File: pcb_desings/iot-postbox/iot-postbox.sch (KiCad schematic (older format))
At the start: 3 parts

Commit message: Added board sch with 2 inputs for restart esp12
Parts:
- removed J?: XLR3_Switched, symbol Connector:XLR3_Switched
- removed U?: WeMos_mini, symbol wemos_mini:WeMos_mini
- added C1: 10uF, Capacitor_SMD:C_0805_2012Metric, symbol Device:C
- added C2: 100nF, Capacitor_SMD:C_0805_2012Metric, symbol Device:C
- added D1, D2, D3: 1N4007, Diode_SMD:D_SOD-123, symbol Device:D
- added J1: Switch_1, Connector_PinHeader_2.54mm:PinHeader_1x02_P2.54mm_Vertical, symbol Connector_Generic:Conn_01x02
- added J2: Switch_2, Connector_PinHeader_2.54mm:PinHeader_1x02_P2.54mm_Vertical, symbol Connector_Generic:Conn_01x02
- added J3: Battery, Connector_PinHeader_2.54mm:PinHeader_1x02_P2.54mm_Vertical, symbol Connector_Generic:Conn_01x02
- added R2, R3, R4, R5, R6, R7: 10k, Resistor_SMD:R_0805_2012Metric, symbol Device:R
- added U1: ESP-12F, RF_Module:ESP-12E, symbol RF_Module:ESP-12F
- R1: footprint (none) -> Resistor_SMD:R_0805_2012Metric
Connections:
- net labels added: +3V3, CH_PD, GPIO12, GPIO13, GPIO14, VCC
- wire segments 9 -> 55
- no-connect marks 0 -> 12

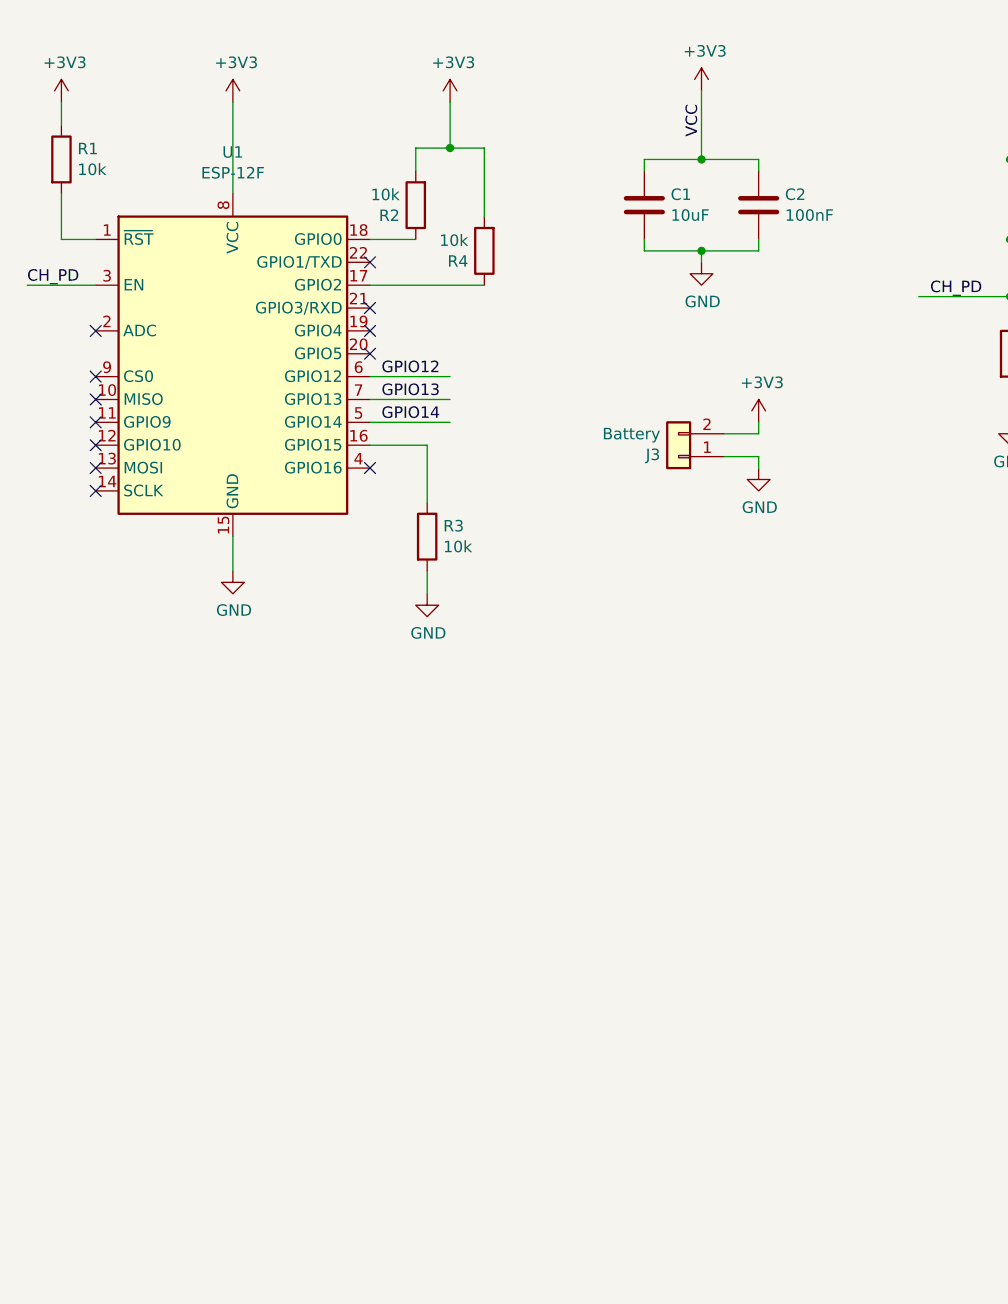
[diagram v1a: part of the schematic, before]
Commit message: Added uart connection to board sch
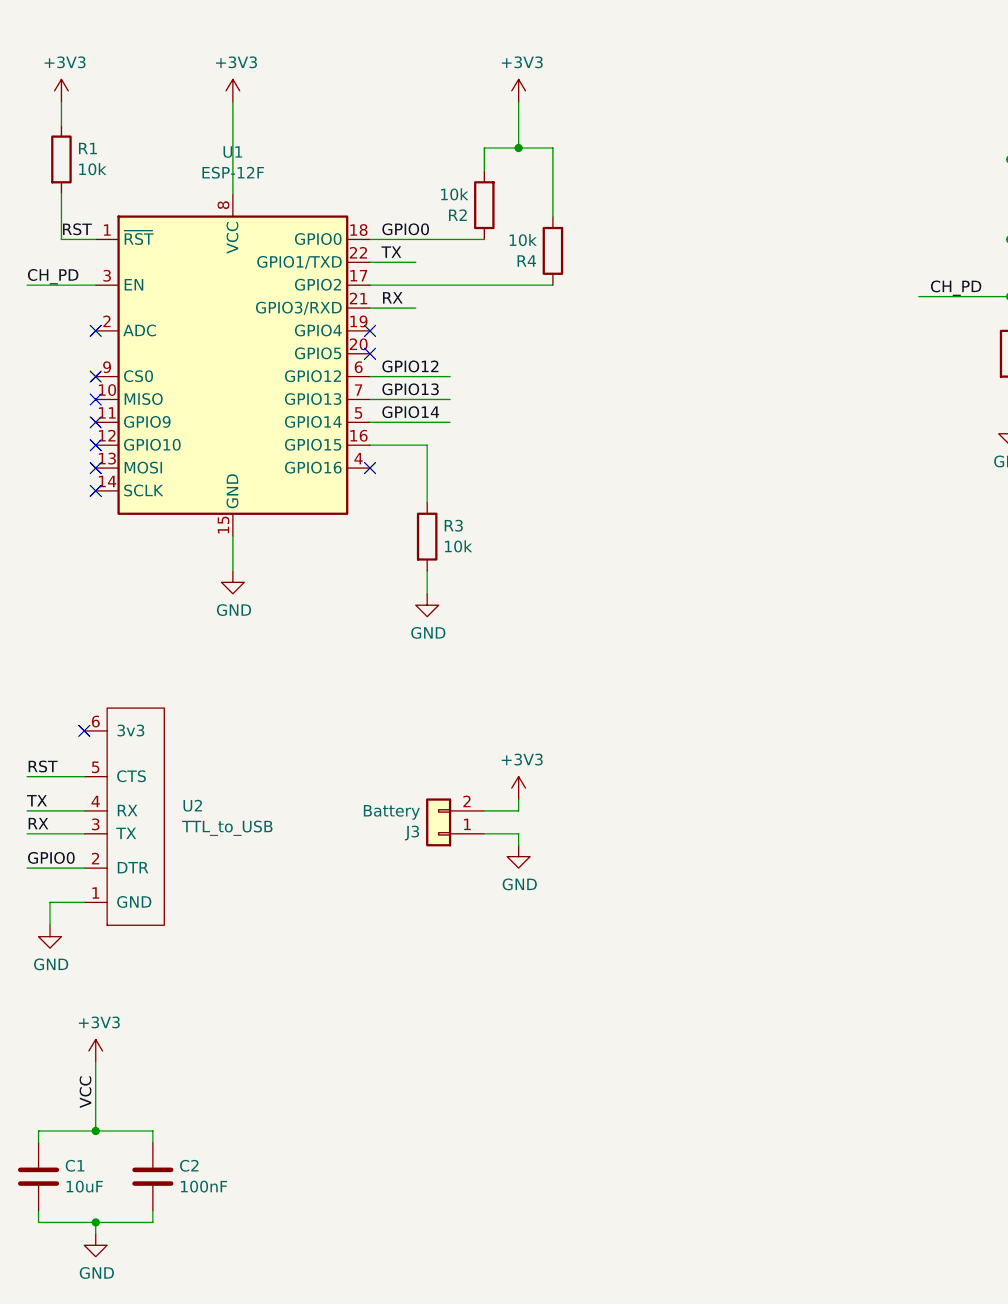
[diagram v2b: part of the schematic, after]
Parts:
- added U2: TTL_to_USB, Connector_PinHeader_2.54mm:PinHeader_1x06_P2.54mm_Vertical, symbol iot-postbox:TTL_to_USB
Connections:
- net labels added: GPIO0, RST, RX, TX
- wire segments 55 -> 63
- no-connect marks 12 -> 11
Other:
- moved on the sheet: C1, C2, J3, R2, R4
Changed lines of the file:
@@
 Comment4 ""
 $EndDescr
-$Comp
-L RF_Module:ESP-12F U1
-U 1 1 60AE687C
-P 1950 2350
-F 0 "U1" H 1950 3331 50  0000 C CNN
-F 1 "ESP-12F" H 1950 3240 50  0000 C CNN
-F 2 "RF_Module:ESP-12E" H 1950 2350 50  0001 C CNN
-F 3 "http://wiki.ai-thinker.com/_media/esp8266/esp8266_series_modules_user_manual_v1.1.pdf" H 1600 2450 50  0001 C CNN
-	1    1950 2350
-	1    0    0    -1
-$EndComp
 Wire Wire Line
 	1350 1950 1050 1950
@@
 L power:+3V3 #PWR06
 U 1 1 60B15876
-P 4000 1100
-F 0 "#PWR06" H 4000 950 50  0001 C CNN
-F 1 "+3V3" H 4015 1273 50  0000 C CNN
-F 2 "" H 4000 1100 50  0001 C CNN
-F 3 "" H 4000 1100 50  0001 C CNN
-	1    4000 1100
+P 1350 5350
+F 0 "#PWR06" H 1350 5200 50  0001 C CNN
+F 1 "+3V3" H 1365 5523 50  0000 C CNN
+F 2 "" H 1350 5350 50  0001 C CNN
+F 3 "" H 1350 5350 50  0001 C CNN
+	1    1350 5350
 	1    0    0    -1
 $EndComp
@@
 Wire Wire Line
 	8150 1950 8150 2150
-Wire Wire Line
-	2550 1750 2750 1750
 $Comp
 L Device:R R2
 U 1 1 60B5027F
-P 2750 1600
-F 0 "R2" H 2820 1646 50  0000 L CNN
-F 1 "10k" H 2820 1555 50  0000 L CNN
-F 2 "Resistor_SMD:R_0805_2012Metric" V 2680 1600 50  0001 C CNN
-F 3 "~" H 2750 1600 50  0001 C CNN
-	1    2750 1600
+P 3050 1600
+F 0 "R2" H 3120 1646 50  0000 L CNN
+F 1 "10k" H 3120 1555 50  0000 L CNN
+F 2 "Resistor_SMD:R_0805_2012Metric" V 2980 1600 50  0001 C CNN
+F 3 "~" H 3050 1600 50  0001 C CNN
+	1    3050 1600
 	-1   0    0    1
 $EndComp
@@
 L Device:R R4
 U 1 1 60B50B9E
-P 3050 1800
-F 0 "R4" H 3120 1846 50  0000 L CNN
-F 1 "10k" H 3120 1755 50  0000 L CNN
-F 2 "Resistor_SMD:R_0805_2012Metric" V 2980 1800 50  0001 C CNN
-F 3 "~" H 3050 1800 50  0001 C CNN
-	1    3050 1800
+P 3350 1800
+F 0 "R4" H 3420 1846 50  0000 L CNN
+F 1 "10k" H 3420 1755 50  0000 L CNN
+F 2 "Resistor_SMD:R_0805_2012Metric" V 3280 1800 50  0001 C CNN
+F 3 "~" H 3350 1800 50  0001 C CNN
+	1    3350 1800
 	-1   0    0    1
 $EndComp
 Wire Wire Line
-	2550 1950 3050 1950
-Wire Wire Line
-	2750 1450 2750 1350
-Wire Wire Line
-	3050 1350 3050 1650
-Wire Wire Line
-	2750 1350 2900 1350
+	3050 1450 3050 1350
+Wire Wire Line
+	3350 1350 3350 1650
+Wire Wire Line
+	3050 1350 3200 1350
 $Comp
 L power:+3V3 #PWR05
 U 1 1 60B58812
-P 2900 1150
-F 0 "#PWR05" H 2900 1000 50  0001 C CNN
-F 1 "+3V3" H 2915 1323 50  0000 C CNN
-F 2 "" H 2900 1150 50  0001 C CNN
-F 3 "" H 2900 1150 50  0001 C CNN
-	1    2900 1150
-	1    0    0    -1
-$EndComp
-Wire Wire Line
-	2900 1150 2900 1350
-Connection ~ 2900 1350
-Wire Wire Line
-	2900 1350 3050 1350
+P 3200 1150
+F 0 "#PWR05" H 3200 1000 50  0001 C CNN
+F 1 "+3V3" H 3215 1323 50  0000 C CNN
+F 2 "" H 3200 1150 50  0001 C CNN
+F 3 "" H 3200 1150 50  0001 C CNN
+	1    3200 1150
+	1    0    0    -1
+$EndComp
+Wire Wire Line
+	3200 1150 3200 1350
+Connection ~ 3200 1350
+Wire Wire Line
+	3200 1350 3350 1350
 $Comp
 L Connector_Generic:Conn_01x02 J2
@@
 	1    0    0    -1
 $EndComp
-Wire Wire Line
-	1950 1550 1950 1150
-Text Label 4000 1300 1    50   ~ 0
+Text Label 1350 5550 1    50   ~ 0
 VCC
 $Comp
 L Device:C C2
 U 1 1 60B72B1E
-P 4250 1600
-F 0 "C2" H 4365 1646 50  0000 L CNN
-F 1 "100nF" H 4365 1555 50  0000 L CNN
-F 2 "Capacitor_SMD:C_0805_2012Metric" H 4288 1450 50  0001 C CNN
-F 3 "~" H 4250 1600 50  0001 C CNN
-	1    4250 1600
-	1    0    0    -1
-$EndComp
-Wire Wire Line
-	4000 1100 4000 1400
-Wire Wire Line
-	4250 1450 4250 1400
-Wire Wire Line
-	4250 1800 4250 1750
+P 1600 5850
+F 0 "C2" H 1715 5896 50  0000 L CNN
+F 1 "100nF" H 1715 5805 50  0000 L CNN
+F 2 "Capacitor_SMD:C_0805_2012Metric" H 1638 5700 50  0001 C CNN
+F 3 "~" H 1600 5850 50  0001 C CNN
+	1    1600 5850
+	1    0    0    -1
+$EndComp
+Wire Wire Line
+	1350 5350 1350 5650
+Wire Wire Line
+	1600 5700 1600 5650
+Wire Wire Line
+	1600 6050 1600 6000
 $Comp
 L power:GND #PWR07
 U 1 1 60B760F1
-P 4000 1850
-F 0 "#PWR07" H 4000 1600 50  0001 C CNN
-F 1 "GND" H 4005 1677 50  0000 C CNN
-F 2 "" H 4000 1850 50  0001 C CNN
-F 3 "" H 4000 1850 50  0001 C CNN
-	1    4000 1850
-	1    0    0    -1
-$EndComp
-Wire Wire Line
-	4000 1850 4000 1800
-Wire Wire Line
-	3750 1750 3750 1800
-Wire Wire Line
-	3750 1450 3750 1400
+P 1350 6100
+F 0 "#PWR07" H 1350 5850 50  0001 C CNN
+F 1 "GND" H 1355 5927 50  0000 C CNN
+F 2 "" H 1350 6100 50  0001 C CNN
+F 3 "" H 1350 6100 50  0001 C CNN
+	1    1350 6100
+	1    0    0    -1
+$EndComp
+Wire Wire Line
+	1350 6100 1350 6050
+Wire Wire Line
+	1100 6000 1100 6050
+Wire Wire Line
+	1100 5700 1100 5650
 $Comp
 L Device:C C1
 U 1 1 60B6FA1D
-P 3750 1600
-F 0 "C1" H 3865 1646 50  0000 L CNN
-F 1 "10uF" H 3865 1555 50  0000 L CNN
-F 2 "Capacitor_SMD:C_0805_2012Metric" H 3788 1450 50  0001 C CNN
-F 3 "~" H 3750 1600 50  0001 C CNN
-	1    3750 1600
-	1    0    0    -1
-$EndComp
-Wire Wire Line
-	3750 1800 4000 1800
-Wire Wire Line
-	3750 1400 4000 1400
-Wire Wire Line
-	4000 1400 4250 1400
-Connection ~ 4000 1400
-Wire Wire Line
-	4000 1800 4250 1800
-Connection ~ 4000 1800
+P 1100 5850
+F 0 "C1" H 1215 5896 50  0000 L CNN
+F 1 "10uF" H 1215 5805 50  0000 L CNN
+F 2 "Capacitor_SMD:C_0805_2012Metric" H 1138 5700 50  0001 C CNN
+F 3 "~" H 1100 5850 50  0001 C CNN
+	1    1100 5850
+	1    0    0    -1
+$EndComp
+Wire Wire Line
+	1100 6050 1350 6050
+Wire Wire Line
+	1100 5650 1350 5650
+Wire Wire Line
+	1350 5650 1600 5650
+Connection ~ 1350 5650
+Wire Wire Line
+	1350 6050 1600 6050
+Connection ~ 1350 6050
 $Comp
 L power:+3V3 #PWR02
@@
 	1    0    0    -1
 $EndComp
-NoConn ~ 2550 1850
-NoConn ~ 2550 2050
 NoConn ~ 2550 2150
 NoConn ~ 2550 2250
@@
 L Connector_Generic:Conn_01x02 J3
 U 1 1 60BC9D92
-P 3900 2700
-F 0 "J3" H 3980 2692 50  0000 L CNN
-F 1 "Battery" H 3980 2601 50  0000 L CNN
-F 2 "Connector_PinHeader_2.54mm:PinHeader_1x02_P2.54mm_Vertical" H 3900 2700 50  0001 C CNN
-F 3 "~" H 3900 2700 50  0001 C CNN
-	1    3900 2700
+P 2850 4350
+F 0 "J3" H 2930 4342 50  0000 L CNN
+F 1 "Battery" H 2930 4251 50  0000 L CNN
+F 2 "Connector_PinHeader_2.54mm:PinHeader_1x02_P2.54mm_Vertical" H 2850 4350 50  0001 C CNN
+F 3 "~" H 2850 4350 50  0001 C CNN
+	1    2850 4350
 	-1   0    0    1
 $EndComp
@@
 L power:+3V3 #PWR013
 U 1 1 60BCAC94
-P 4250 2550
-F 0 "#PWR013" H 4250 2400 50  0001 C CNN
-F 1 "+3V3" H 4265 2723 50  0000 C CNN
-F 2 "" H 4250 2550 50  0001 C CNN
-F 3 "" H 4250 2550 50  0001 C CNN
-	1    4250 2550
+P 3200 4200
+F 0 "#PWR013" H 3200 4050 50  0001 C CNN
+F 1 "+3V3" H 3215 4373 50  0000 C CNN
+F 2 "" H 3200 4200 50  0001 C CNN
+F 3 "" H 3200 4200 50  0001 C CNN
+	1    3200 4200
 	1    0    0    -1
 $EndComp
@@
 L power:GND #PWR014
 U 1 1 60BCB652
-P 4250 2750
-F 0 "#PWR014" H 4250 2500 50  0001 C CNN
-F 1 "GND" H 4255 2577 50  0000 C CNN
-F 2 "" H 4250 2750 50  0001 C CNN
-F 3 "" H 4250 2750 50  0001 C CNN
-	1    4250 2750
-	1    0    0    -1
-$EndComp
-Wire Wire Line
-	4100 2600 4250 2600
-Wire Wire Line
-	4250 2600 4250 2550
-Wire Wire Line
-	4250 2750 4250 2700
-Wire Wire Line
-	4250 2700 4100 2700
+P 3200 4400
+F 0 "#PWR014" H 3200 4150 50  0001 C CNN
+F 1 "GND" H 3205 4227 50  0000 C CNN
+F 2 "" H 3200 4400 50  0001 C CNN
+F 3 "" H 3200 4400 50  0001 C CNN
+	1    3200 4400
+	1    0    0    -1
+$EndComp
+Wire Wire Line
+	3050 4250 3200 4250
+Wire Wire Line
+	3200 4250 3200 4200
+Wire Wire Line
+	3200 4400 3200 4350
+Wire Wire Line
+	3200 4350 3050 4350
+$Comp
+L iot-postbox:TTL_to_USB U2
+U 1 1 60B4E2F6
+P 1550 4750
+F 0 "U2" H 1728 5271 50  0000 L CNN
+F 1 "TTL_to_USB" H 1728 5180 50  0000 L CNN
+F 2 "Connector_PinHeader_2.54mm:PinHeader_1x06_P2.54mm_Vertical" H 1350 4800 50  0001 C CNN
+F 3 "" H 1350 4800 50  0001 C CNN
+	1    1550 4750
+	1    0    0    -1
+$EndComp
+Wire Wire Line
+	1300 4100 1050 4100
+Wire Wire Line
+	1300 4250 1050 4250
+Wire Wire Line
+	1300 4350 1050 4350
+Wire Wire Line
+	1300 4500 1050 4500
+Wire Wire Line
+	1300 4650 1150 4650
+NoConn ~ 1300 3900
+Text Label 1200 1750 0    50   ~ 0
+RST
+Text Label 1050 4100 0    50   ~ 0
+RST
+$Comp
+L RF_Module:ESP-12F U1
+U 1 1 60AE687C
+P 1950 2350
+F 0 "U1" H 1950 3331 50  0000 C CNN
+F 1 "ESP-12F" H 1950 3240 50  0000 C CNN
+F 2 "RF_Module:ESP-12E" H 1950 2350 50  0001 C CNN
+F 3 "http://wiki.ai-thinker.com/_media/esp8266/esp8266_series_modules_user_manual_v1.1.pdf" H 1600 2450 50  0001 C CNN
+	1    1950 2350
+	1    0    0    -1
+$EndComp
+Wire Wire Line
+	2550 1850 2750 1850
+Wire Wire Line
+	2550 2050 2750 2050
+Text Label 2600 1850 0    50   ~ 0
+TX
+Text Label 2600 2050 0    50   ~ 0
+RX
+Text Label 1050 4350 0    50   ~ 0
+RX
+Text Label 1050 4250 0    50   ~ 0
+TX
+Text Label 2600 1750 0    50   ~ 0
+GPIO0
+Wire Wire Line
+	2550 1750 3050 1750
+Wire Wire Line
+	2550 1950 3350 1950
+Text Label 1050 4500 0    50   ~ 0
+GPIO0
+$Comp
+L power:GND #PWR0101
+U 1 1 60B68C08
+P 1150 4750
+F 0 "#PWR0101" H 1150 4500 50  0001 C CNN
+F 1 "GND" H 1155 4577 50  0000 C CNN
+F 2 "" H 1150 4750 50  0001 C CNN
+F 3 "" H 1150 4750 50  0001 C CNN
+	1    1150 4750
+	1    0    0    -1
+$EndComp
+Wire Wire Line
+	1150 4750 1150 4650
+Wire Wire Line
+	1950 1550 1950 1150
 $EndSCHEMATC

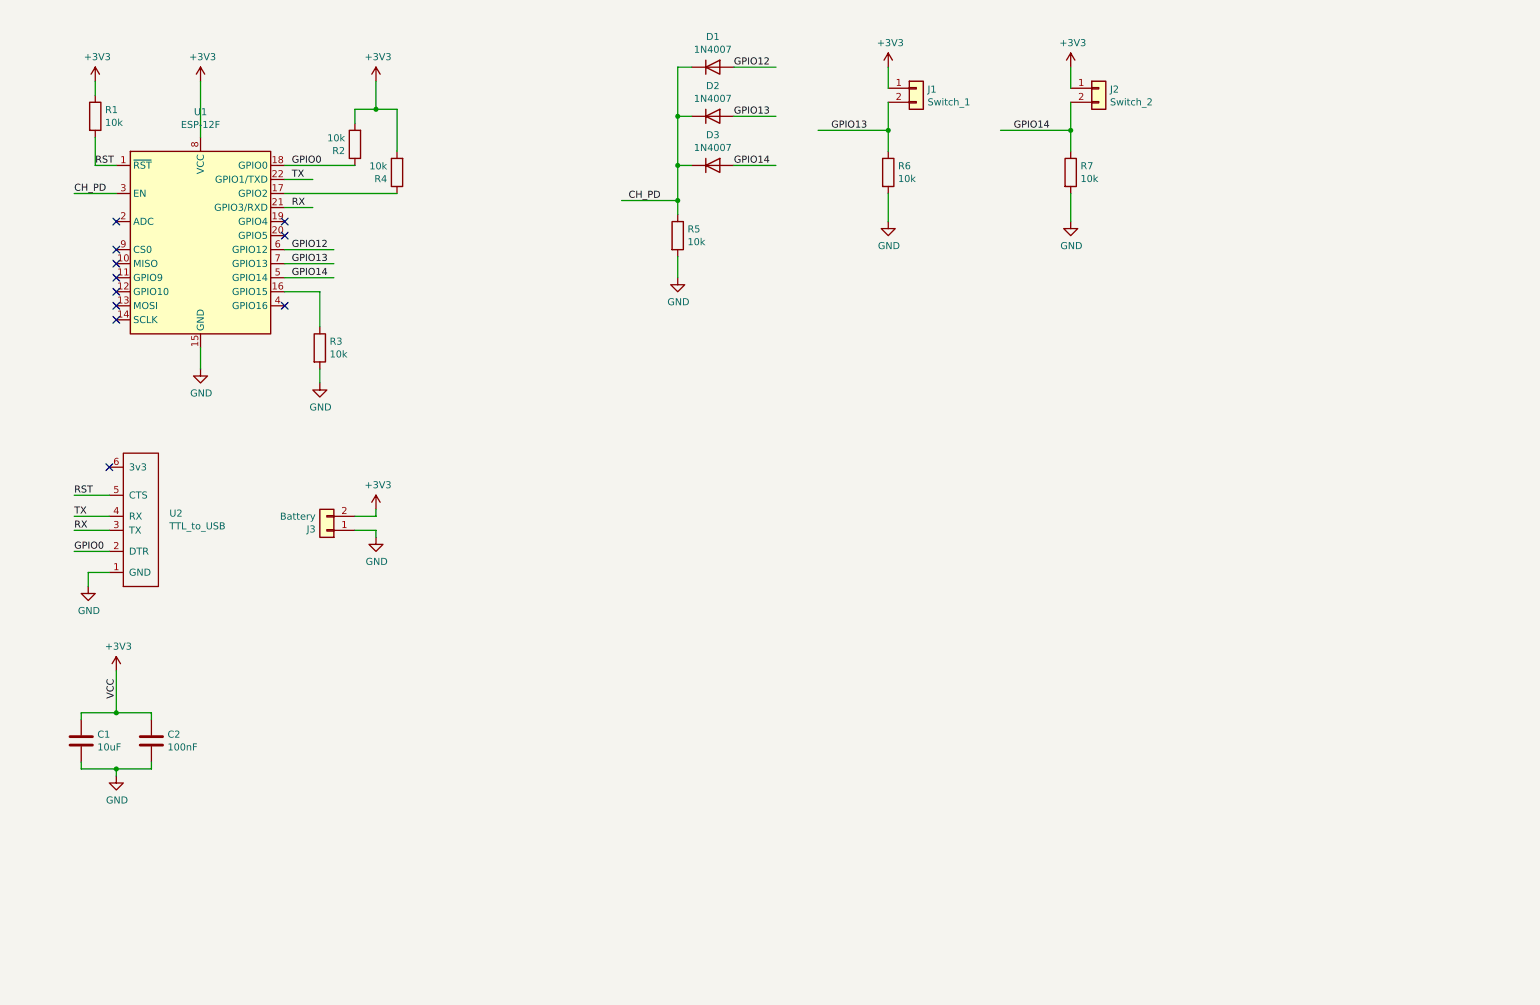
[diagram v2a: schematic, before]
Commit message: Added PostBox functions to setup 2 pins interrupts and mqtt mesage publish
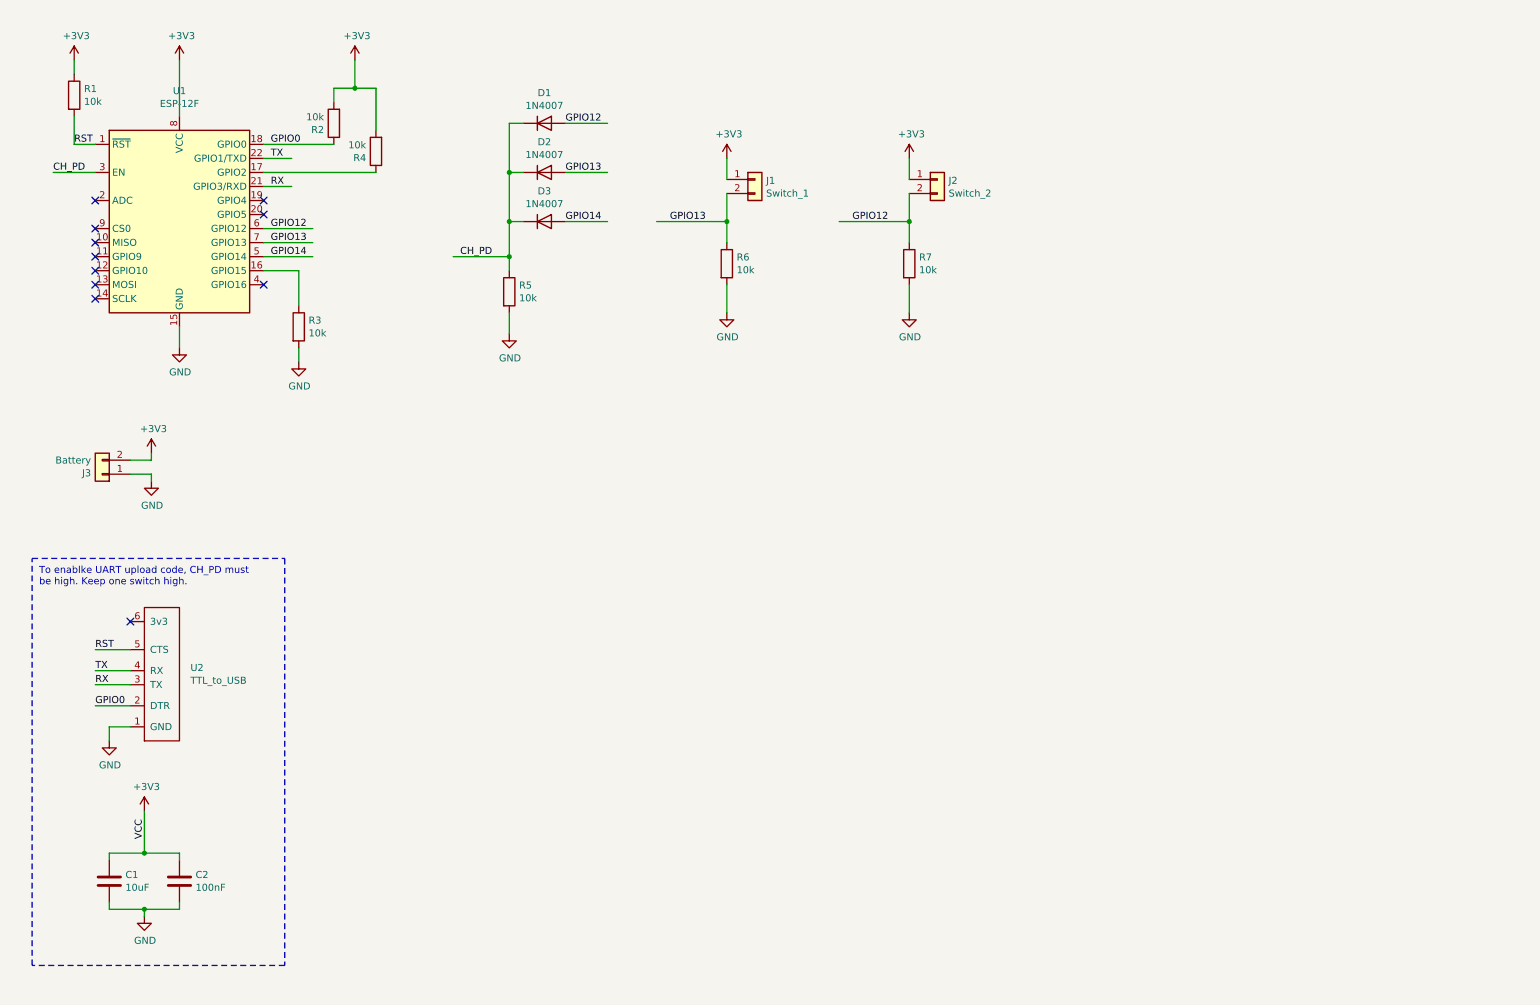
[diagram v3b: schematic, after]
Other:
- note added: "To enablke UART upload code, CH_PD must \nbe high. Keep one switch high.\n"
- moved on the sheet: C1, C2, D1, D2, D3, J1, J2, J3, R1, R2, R3, R4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
